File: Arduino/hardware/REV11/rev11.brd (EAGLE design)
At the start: 79 x 79 mm, 26 parts, among them IC2 ATMEGA168-AU, Q1 32768Hz

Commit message: updated rev11 as per mark & damons spec's
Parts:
- removed FTDI+I2C: (no value), pinhead:2X07
- added I2C_EXT: (no value), pinhead:2X07
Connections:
- removed net N$5: FTDI+I2C.9, R4.2
- new net N$4: I2C_EXT.11, R4.2
- net GND: now also I2C_EXT.6; no longer FTDI+I2C.1, FTDI+I2C.3
- net N$1: now also I2C_EXT.5; no longer FTDI+I2C.11
- net N$3: now also I2C_EXT.12; no longer FTDI+I2C.7
- net RFM_IRQ: now also I2C_EXT.7
- net SCL: now also I2C_EXT.9; no longer FTDI+I2C.2
- net SDA: now also I2C_EXT.10; no longer FTDI+I2C.4
- net SPI_MISO: now also I2C_EXT.1
- net SPI_MOSI: now also I2C_EXT.4
- net SPI_NSS: now also I2C_EXT.8
- net SPI_SCK: now also I2C_EXT.3
- net VCC: now also I2C_EXT.2; no longer FTDI+I2C.14

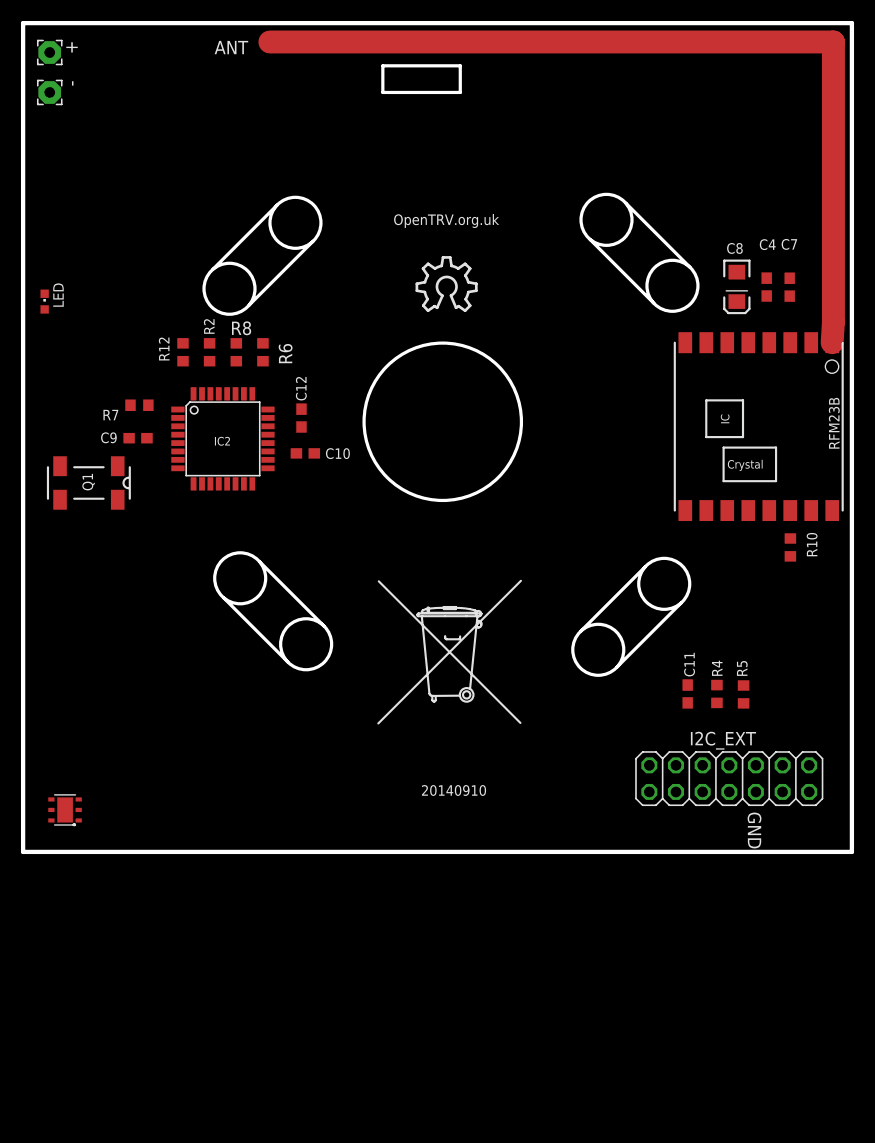
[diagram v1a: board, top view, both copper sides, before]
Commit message: updated rev11 as per mark and damon spec 2
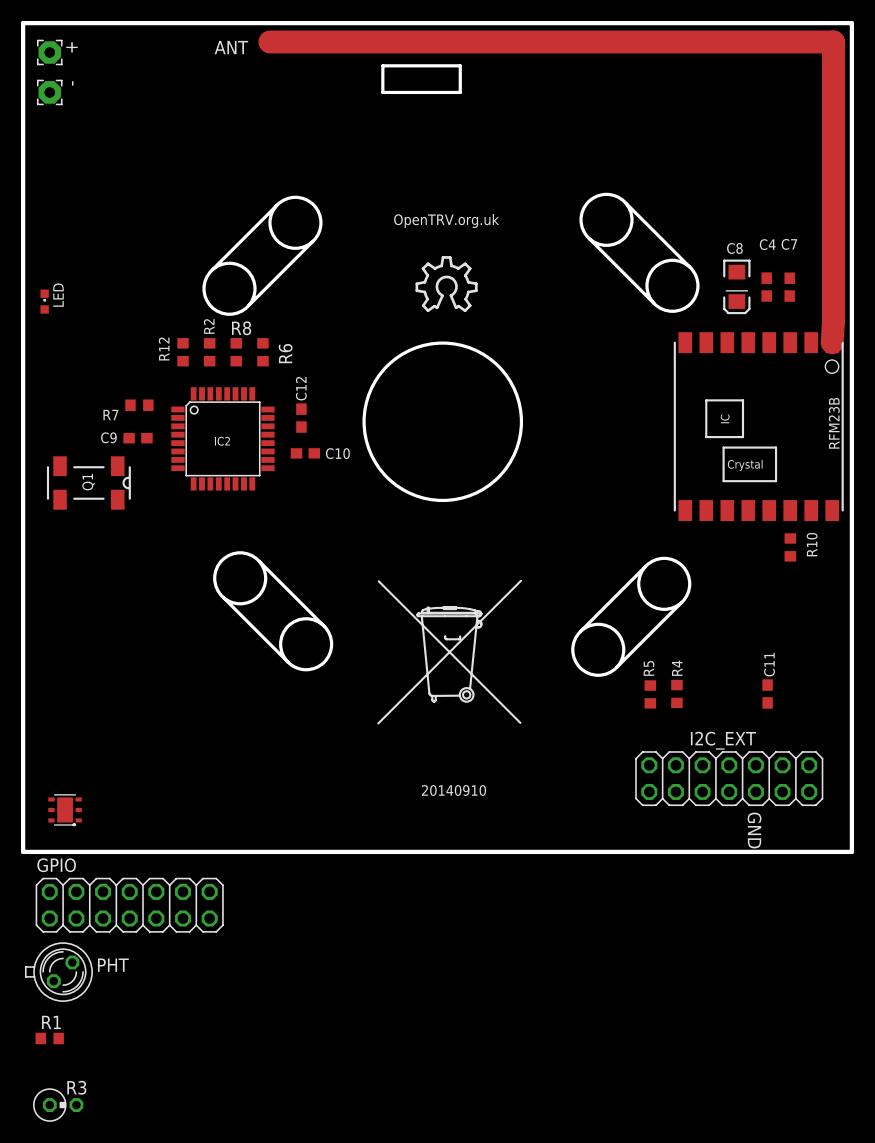
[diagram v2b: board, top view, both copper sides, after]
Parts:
- added GPIO: (no value), pinhead:2X07
- added PHT: BPX65, opto-trans-siemens:BPX65
- added R1: 220K, resistor:R0603
- added R3: (no value), resistor:0309V
- moved R5 8.89 mm to (59.8, 15.0)
- moved C11 7.62 mm to (71.0, 15.1)
- moved R4 3.81 mm to (62.3, 15.1)
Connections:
- net LED renamed LED_HEATCALL_L
- removed net A0: IC2.23
- removed net D8: IC2.12
- new net IO_POWER_UP: IC2.12, PHT.K
- new net LDR: IC2.23, PHT.A, R1.1, R3.2
- net GND: now also R1.2, R3.1
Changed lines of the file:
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@@
 <attribute name="NAME" x="28.79625" y="37.4661" size="1" layer="25" font="vector" ratio="10"/>
 </element>
-<element name="R4" library="resistor" package="R0603" value="4.7K" x="66.135875" y="15.0529125" smashed="yes" rot="R270">
-<attribute name="NAME" x="66.664153125" y="16.658984375" size="1" layer="25" font="vector" ratio="10" rot="R90"/>
-</element>
-<element name="R5" library="resistor" package="R0603" value="4.7K" x="68.677090625" y="15.0070875" smashed="yes" rot="R270">
-<attribute name="NAME" x="69.041478125" y="16.658984375" size="1" layer="25" font="vector" ratio="10" rot="R90"/>
-</element>
-<element name="C11" library="resistor" package="C0603" value="100nF" x="63.343821875" y="15.0529125" smashed="yes" rot="R270">
-<attribute name="NAME" x="64.023653125" y="16.658984375" size="1" layer="25" font="vector" ratio="10" rot="R90"/>
+<element name="R4" library="resistor" package="R0603" value="4.7K" x="62.325875" y="15.0529125" smashed="yes" rot="R270">
+<attribute name="NAME" x="62.854153125" y="16.658984375" size="1" layer="25" font="vector" ratio="10" rot="R90"/>
+</element>
+<element name="R5" library="resistor" package="R0603" value="4.7K" x="59.787090625" y="15.0070875" smashed="yes" rot="R270">
+<attribute name="NAME" x="60.151478125" y="16.658984375" size="1" layer="25" font="vector" ratio="10" rot="R90"/>
+</element>
+<element name="C11" library="resistor" package="C0603" value="100nF" x="70.963821875" y="15.0529125" smashed="yes" rot="R270">
+<attribute name="NAME" x="71.643653125" y="16.658984375" size="1" layer="25" font="vector" ratio="10" rot="R90"/>
 </element>
 <element name="U$1" library="ohw-logo" package="OSHW_10X200_NOTEXT" value="" x="37.534165625" y="51.58610625"/>
@@
 <element name="+" library="wirepad" package="2,15/1,0" value="" x="2.54" y="76.2" rot="R270"/>
 <element name="-" library="wirepad" package="2,15/1,0" value="" x="2.54" y="72.39" rot="R270"/>
+<element name="GPIO" library="pinhead" package="2X07" value="" x="10.16" y="-5.08"/>
+<element name="R1" library="resistor" package="R0603" value="220K" x="2.54" y="-17.78"/>
+<element name="PHT" library="opto-trans-siemens" package="BPX65" value="BPX65" x="3.81" y="-11.43">
+<attribute name="OC_NEWARK" value="06WX2764" x="3.81" y="-17.78" size="1.778" layer="27" display="off"/>
+<attribute name="OC_FARNELL" value="327451" x="3.81" y="-17.78" size="1.778" layer="27" display="off"/>
+<attribute name="MF" value="" x="3.81" y="-17.78" size="1.778" layer="27" display="off"/>
+<attribute name="MPN" value="BPX65." x="3.81" y="-17.78" size="1.778" layer="27" display="off"/>
+</element>
+<element name="R3" library="resistor" package="0309V" value="" x="3.81" y="-24.13"/>
 </elements>
 <signals>
@@
 <contactref element="-" pad="1"/>
 <contactref element="I2C_EXT" pad="6"/>
+<contactref element="R1" pad="2"/>
+<contactref element="R3" pad="1"/>
 <wire x1="70.879840625" y1="54.6883" x2="73.07053125" y2="54.67946875" width="0" layer="19" extent="1-1"/>
 <wire x1="68.03278125" y1="55.259175" x2="70.879840625" y2="54.6883" width="0" layer="19" extent="1-1"/>
@@
 <wire x1="5.3" y1="4" x2="11.803065625" y2="39.436453125" width="0" layer="19" extent="1-1"/>
 <wire x1="4" y1="4" x2="5.3" y2="4" width="0" layer="19" extent="1-1"/>
+<wire x1="3.39" y1="-17.78" x2="4" y2="4" width="0" layer="19" extent="1-1"/>
+<wire x1="2.54" y1="-24.13" x2="3.39" y2="-17.78" width="0" layer="19" extent="1-1"/>
 </signal>
 <signal name="D6">
@@
 <contactref element="C11" pad="1"/>
 <contactref element="IC2" pad="29"/>
-<wire x1="17.78" y1="46.775" x2="63.343821875" y2="15.9029125" width="0" layer="19" extent="16-16"/>
+<wire x1="17.78" y1="46.775" x2="70.963821875" y2="15.9029125" width="0" layer="19" extent="16-16"/>
 <wire x1="18.65" y1="43.6626" x2="17.78" y2="46.775" width="0" layer="19" extent="1-16"/>
 </signal>
@@
 <contactref element="R5" pad="1"/>
 <contactref element="IC2" pad="30"/>
-<wire x1="17.85" y1="43.6626" x2="68.677090625" y2="15.8570875" width="0" layer="19" extent="1-16"/>
+<wire x1="17.85" y1="43.6626" x2="59.787090625" y2="15.8570875" width="0" layer="19" extent="1-16"/>
 </signal>
 <signal name="RX">
 <contactref element="R4" pad="1"/>
 <contactref element="IC2" pad="31"/>
-<wire x1="17.05" y1="43.6626" x2="66.135875" y2="15.9029125" width="0" layer="19" extent="1-16"/>
+<wire x1="17.05" y1="43.6626" x2="62.325875" y2="15.9029125" width="0" layer="19" extent="1-16"/>
 </signal>
 <signal name="N$1">
 <contactref element="C11" pad="2"/>
 <contactref element="I2C_EXT" pad="5"/>
-<wire x1="63.343821875" y1="14.2029125" x2="69.85" y2="8.255" width="0" layer="19" extent="1-1"/>
+<wire x1="70.963821875" y1="14.2029125" x2="69.85" y2="8.255" width="0" layer="19" extent="1-1"/>
 </signal>
 <signal name="N$2">
@@
 <contactref element="R5" pad="2"/>
 <contactref element="I2C_EXT" pad="12"/>
-<wire x1="62.23" y1="5.715" x2="68.677090625" y2="14.1570875" width="0" layer="19" extent="1-1"/>
+<wire x1="62.23" y1="5.715" x2="59.787090625" y2="14.1570875" width="0" layer="19" extent="1-1"/>
 </signal>
 <signal name="N$23">
@@
 <wire x1="24.765" y1="77.2" x2="24.765" y2="76.835" width="0.4064" layer="1"/>
 </signal>
-<signal name="A0">
-<contactref element="IC2" pad="23"/>
-</signal>
 <signal name="A2">
 <contactref element="IC2" pad="25"/>
@@
 <contactref element="IC2" pad="9"/>
 </signal>
-<signal name="D8">
-<contactref element="IC2" pad="12"/>
-</signal>
 <signal name="D2">
 <contactref element="IC2" pad="32"/>
@@
 <contactref element="IC2" pad="22"/>
 </signal>
-<signal name="LED">
+<signal name="LED_HEATCALL_L">
 <contactref element="IC2" pad="2"/>
 <contactref element="R7" pad="1"/>
@@
 <contactref element="R4" pad="2"/>
 <contactref element="I2C_EXT" pad="11"/>
-<wire x1="62.23" y1="8.255" x2="66.135875" y2="14.2029125" width="0" layer="19" extent="1-1"/>
+<wire x1="62.23" y1="8.255" x2="62.325875" y2="14.2029125" width="0" layer="19" extent="1-1"/>
+</signal>
+<signal name="LDR">
+<contactref element="R1" pad="1"/>
+<contactref element="PHT" pad="A"/>
+<contactref element="R3" pad="2"/>
+<contactref element="IC2" pad="23"/>
+<wire x1="2.921" y1="-12.319" x2="23.3426" y2="41.37" width="0" layer="19" extent="1-1"/>
+<wire x1="1.69" y1="-17.78" x2="2.921" y2="-12.319" width="0" layer="19" extent="1-1"/>
+<wire x1="5.08" y1="-24.13" x2="1.69" y2="-17.78" width="0" layer="19" extent="1-1"/>
+</signal>
+<signal name="IO_POWER_UP" class="1">
+<contactref element="PHT" pad="K"/>
+<contactref element="IC2" pad="12"/>
+<wire x1="4.699" y1="-10.541" x2="18.65" y2="35.0774" width="0" layer="19" extent="1-1"/>
 </signal>
 </signals>

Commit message: added gpio this time
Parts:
- removed GPIO: (no value), pinhead:2X07
- added DQ: (no value), wirepad:2,15/1,0
- added JP1: (no value), pinhead:1X09
- added R9: 4.7K, resistor:R0603
- moved R3 36.8 mm to (3.81, 12.7), turned to 180 degrees
- moved R1 34.3 mm to (3.81, 16.5)
- moved PHT 34.3 mm to (3.81, 22.9), turned to 180 degrees
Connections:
- net A1: now also JP1.1
- net A2: now also JP1.2
- net A3: now also JP1.3
- net A6: now also JP1.4
- net A7: now also JP1.5
- net D2: now also DQ.1, R9.1
- net D3: now also JP1.6
- net D5: now also JP1.7
- net D6: now also JP1.8
- net D7: now also JP1.9
- net VCC: now also R9.2
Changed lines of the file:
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@@
 <board>
 <plain>
-<text x="44.211028125" y="6.35376875" size="1" layer="25" font="vector" ratio="10" rot="R180">20140910</text>
+<text x="44.211028125" y="11.43376875" size="1" layer="25" font="vector" ratio="10" rot="R180">20140910</text>
 <text x="27.920803125" y="1.684378125" size="1" layer="22" font="vector" ratio="10" rot="MR180">License: http://goo.gl/3d71UJ</text>
 <text x="35.291121875" y="59.76046875" size="1" layer="25" font="vector" ratio="10">OpenTRV.org.uk</text>
@@
 <element name="+" library="wirepad" package="2,15/1,0" value="" x="2.54" y="76.2" rot="R270"/>
 <element name="-" library="wirepad" package="2,15/1,0" value="" x="2.54" y="72.39" rot="R270"/>
-<element name="GPIO" library="pinhead" package="2X07" value="" x="10.16" y="-5.08"/>
-<element name="R1" library="resistor" package="R0603" value="220K" x="2.54" y="-17.78"/>
-<element name="PHT" library="opto-trans-siemens" package="BPX65" value="BPX65" x="3.81" y="-11.43">
-<attribute name="OC_NEWARK" value="06WX2764" x="3.81" y="-17.78" size="1.778" layer="27" display="off"/>
-<attribute name="OC_FARNELL" value="327451" x="3.81" y="-17.78" size="1.778" layer="27" display="off"/>
-<attribute name="MF" value="" x="3.81" y="-17.78" size="1.778" layer="27" display="off"/>
-<attribute name="MPN" value="BPX65." x="3.81" y="-17.78" size="1.778" layer="27" display="off"/>
-</element>
-<element name="R3" library="resistor" package="0309V" value="" x="3.81" y="-24.13"/>
+<element name="R1" library="resistor" package="R0603" value="220K" x="3.81" y="16.51" smashed="yes">
+<attribute name="NAME" x="2.921" y="17.399" size="1.27" layer="25"/>
+</element>
+<element name="PHT" library="opto-trans-siemens" package="BPX65" value="BPX65" x="3.81" y="22.86" smashed="yes" rot="R180">
+<attribute name="OC_NEWARK" value="06WX2764" x="3.81" y="29.21" size="1.778" layer="27" rot="R180" display="off"/>
+<attribute name="OC_FARNELL" value="327451" x="3.81" y="29.21" size="1.778" layer="27" rot="R180" display="off"/>
+<attribute name="MF" value="" x="3.81" y="29.21" size="1.778" layer="27" rot="R180" display="off"/>
+<attribute name="MPN" value="BPX65." x="3.81" y="29.21" size="1.778" layer="27" rot="R180" display="off"/>
+<attribute name="NAME" x="5.715" y="27.94" size="1.27" layer="25" ratio="10" rot="R180"/>
+</element>
+<element name="R3" library="resistor" package="0309V" value="" x="3.81" y="12.7" rot="R180"/>
+<element name="R9" library="resistor" package="R0603" value="4.7K" x="17.78" y="12.7" smashed="yes" rot="R180">
+<attribute name="NAME" x="18.669" y="11.811" size="1.27" layer="25" rot="R180"/>
+</element>
+<element name="DQ" library="wirepad" package="2,15/1,0" value="" x="25.4" y="5.08"/>
+<element name="JP1" library="pinhead" package="1X09" value="" x="40.64" y="5.08" smashed="yes" rot="R180">
+<attribute name="NAME" x="41.3512" y="8.9662" size="1.27" layer="25" ratio="10" rot="R180"/>
+<attribute name="VALUE" x="52.07" y="8.89" size="1.27" layer="27" rot="R180"/>
+</element>
 </elements>
 <signals>
@@
 <contactref element="+" pad="1"/>
 <contactref element="I2C_EXT" pad="2"/>
+<contactref element="R9" pad="2"/>
 <wire x1="70.879840625" y1="52.9883" x2="73.07053125" y2="52.97946875" width="0" layer="19" extent="1-1"/>
 <wire x1="68.03278125" y1="52.459175" x2="70.879840625" y2="52.9883" width="0" layer="19" extent="1-1"/>
@@
 <wire x1="2.54" y1="76.2" x2="2.05" y2="51.705" width="0" layer="19" extent="1-1"/>
 <wire x1="2.7" y1="4" x2="10.103065625" y2="39.436453125" width="0" layer="19" extent="1-1"/>
+<wire x1="16.93" y1="12.7" x2="2.7" y2="4" width="0" layer="19" extent="1-1"/>
 <wire x1="74.93" y1="5.715" x2="69.12" y2="48.54" width="0" layer="19" extent="1-1"/>
 </signal>
@@
 <wire x1="5.3" y1="4" x2="11.803065625" y2="39.436453125" width="0" layer="19" extent="1-1"/>
 <wire x1="4" y1="4" x2="5.3" y2="4" width="0" layer="19" extent="1-1"/>
-<wire x1="3.39" y1="-17.78" x2="4" y2="4" width="0" layer="19" extent="1-1"/>
-<wire x1="2.54" y1="-24.13" x2="3.39" y2="-17.78" width="0" layer="19" extent="1-1"/>
+<wire x1="4.66" y1="16.51" x2="4" y2="4" width="0" layer="19" extent="1-1"/>
+<wire x1="5.08" y1="12.7" x2="4.66" y2="16.51" width="0" layer="19" extent="1-1"/>
 </signal>
 <signal name="D6">
 <contactref element="IC2" pad="10"/>
+<contactref element="JP1" pad="8"/>
+<wire x1="33.02" y1="5.08" x2="17.05" y2="35.0774" width="0" layer="19" extent="1-1"/>
 </signal>
 <signal name="SPI_SCK">
@@
 <signal name="A2">
 <contactref element="IC2" pad="25"/>
+<contactref element="JP1" pad="2"/>
+<wire x1="48.26" y1="5.08" x2="21.85" y2="43.6626" width="0" layer="19" extent="1-1"/>
 </signal>
 <signal name="D5">
 <contactref element="IC2" pad="9"/>
+<contactref element="JP1" pad="7"/>
+<wire x1="35.56" y1="5.08" x2="16.25" y2="35.0774" width="0" layer="19" extent="1-1"/>
 </signal>
 <signal name="D2">
 <contactref element="IC2" pad="32"/>
+<contactref element="R9" pad="1"/>
+<contactref element="DQ" pad="1"/>
+<wire x1="18.63" y1="12.7" x2="16.25" y2="43.6626" width="0" layer="19" extent="1-1"/>
+<wire x1="25.4" y1="5.08" x2="18.63" y2="12.7" width="0" layer="19" extent="1-1"/>
 </signal>
 <signal name="D7">
 <contactref element="IC2" pad="11"/>
+<contactref element="JP1" pad="9"/>
+<wire x1="30.48" y1="5.08" x2="17.85" y2="35.0774" width="0" layer="19" extent="1-1"/>
 </signal>
 <signal name="A1">
 <contactref element="IC2" pad="24"/>
+<contactref element="JP1" pad="1"/>
+<wire x1="50.8" y1="5.08" x2="23.3426" y2="42.17" width="0" layer="19" extent="1-1"/>
 </signal>
 <signal name="D3">
 <contactref element="IC2" pad="1"/>
+<contactref element="JP1" pad="6"/>
+<wire x1="38.1" y1="5.08" x2="14.7574" y2="42.17" width="0" layer="19" extent="1-1"/>
 </signal>
 <signal name="A3">
 <contactref element="IC2" pad="26"/>
+<contactref element="JP1" pad="3"/>
+<wire x1="45.72" y1="5.08" x2="21.05" y2="43.6626" width="0" layer="19" extent="1-1"/>
 </signal>
 <signal name="A6">
 <contactref element="IC2" pad="19"/>
+<contactref element="JP1" pad="4"/>
+<wire x1="43.18" y1="5.08" x2="23.3426" y2="38.17" width="0" layer="19" extent="1-1"/>
 </signal>
 <signal name="A7">
 <contactref element="IC2" pad="22"/>
+<contactref element="JP1" pad="5"/>
+<wire x1="40.64" y1="5.08" x2="23.3426" y2="40.57" width="0" layer="19" extent="1-1"/>
 </signal>
 <signal name="LED_HEATCALL_L">
@@
 <contactref element="R3" pad="2"/>
 <contactref element="IC2" pad="23"/>
-<wire x1="2.921" y1="-12.319" x2="23.3426" y2="41.37" width="0" layer="19" extent="1-1"/>
-<wire x1="1.69" y1="-17.78" x2="2.921" y2="-12.319" width="0" layer="19" extent="1-1"/>
-<wire x1="5.08" y1="-24.13" x2="1.69" y2="-17.78" width="0" layer="19" extent="1-1"/>
+<wire x1="4.699" y1="23.749" x2="23.3426" y2="41.37" width="0" layer="19" extent="1-1"/>
+<wire x1="2.96" y1="16.51" x2="4.699" y2="23.749" width="0" layer="19" extent="1-1"/>
+<wire x1="2.54" y1="12.7" x2="2.96" y2="16.51" width="0" layer="19" extent="1-1"/>
 </signal>
 <signal name="IO_POWER_UP" class="1">
 <contactref element="PHT" pad="K"/>
 <contactref element="IC2" pad="12"/>
-<wire x1="4.699" y1="-10.541" x2="18.65" y2="35.0774" width="0" layer="19" extent="1-1"/>
+<wire x1="2.921" y1="21.971" x2="18.65" y2="35.0774" width="0" layer="19" extent="1-1"/>
 </signal>
 </signals>
